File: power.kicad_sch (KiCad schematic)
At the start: 72 parts, among them J5 Molex_Mini-Fit-Jr_2x4_39-28-8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, Q1 DMPH4029LFGQ, Q12 SI7613DN-T1-GE3, Q13 SI7613DN-T1-GE3, Q2 BSS138-7-F, Q3 BSS138-7-F, U1 TPS56C230, U7 LTC4412IS6, U8 LTC4412IS6, U9 SIC477ED-T1-GE3

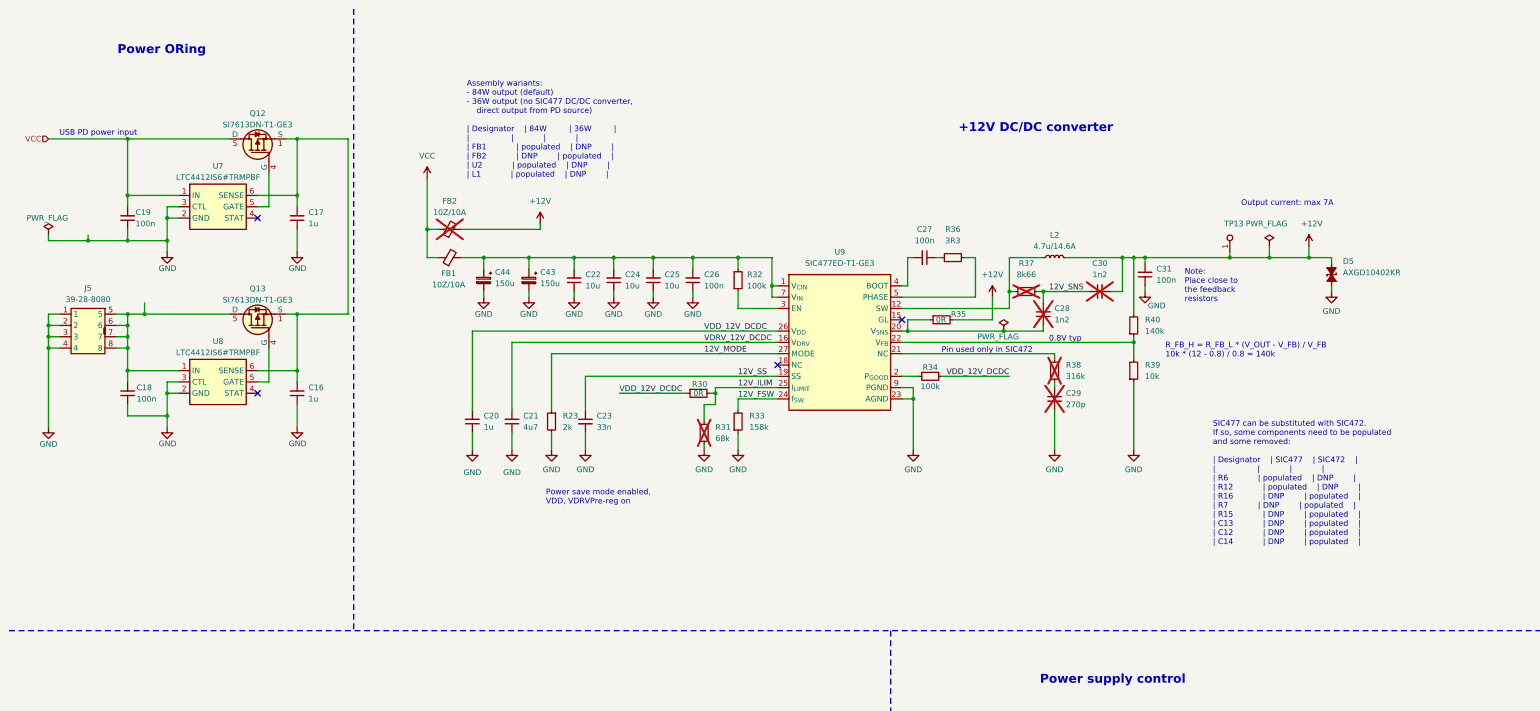
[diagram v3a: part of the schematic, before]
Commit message: [#79262] Move ideal diodes and Molex connector to separate schematic sheet
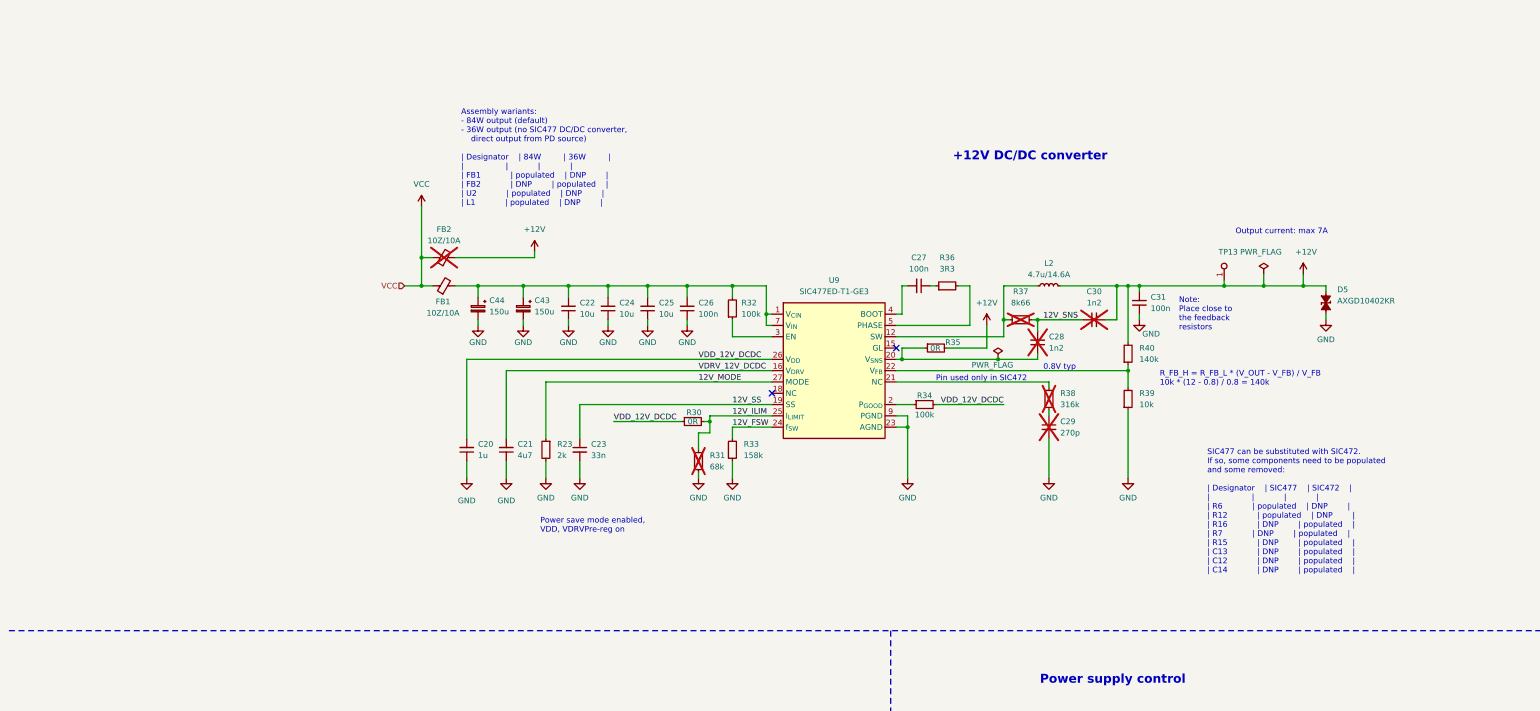
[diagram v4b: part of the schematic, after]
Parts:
- removed C16, C17: C_1u_25V_0603, antmicro-footprints:C_0603_1608Metric, symbol antmicroCapacitors0603:C_1u_25V_0603
- removed C18, C19: C_100n_0402, antmicro-footprints:C_0402_1005Metric, symbol antmicroCapacitors0402:C_100n_0402
- removed J5: Molex_Mini-Fit-Jr_2x4_39-28-8080, antmicro-footprints:MOLEX_39288080, symbol antmicroWire2BoardConnectors:Molex_Mini-Fit-Jr_2x4_39-28-8080
- removed Q12, Q13: SI7613DN-T1-GE3, antmicro-footprints:Vishay_PowerPAK_1212-8_Single, symbol antmicroTransistorsFETsMOSFETsSingle:SI7613DN-T1-GE3
- removed U7, U8: LTC4412IS6, antmicro-footprints:SOT-23-6, symbol antmicroPMICORControllersIdealDiodes:LTC4412IS6
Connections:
- no-connect marks 5 -> 3
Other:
- note removed: "Power ORing"
- note removed: "USB PD power input"
- moved on the sheet: C20, C21, C22, C23, C24, C25, C26, C27, C28, C29, C30, C31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

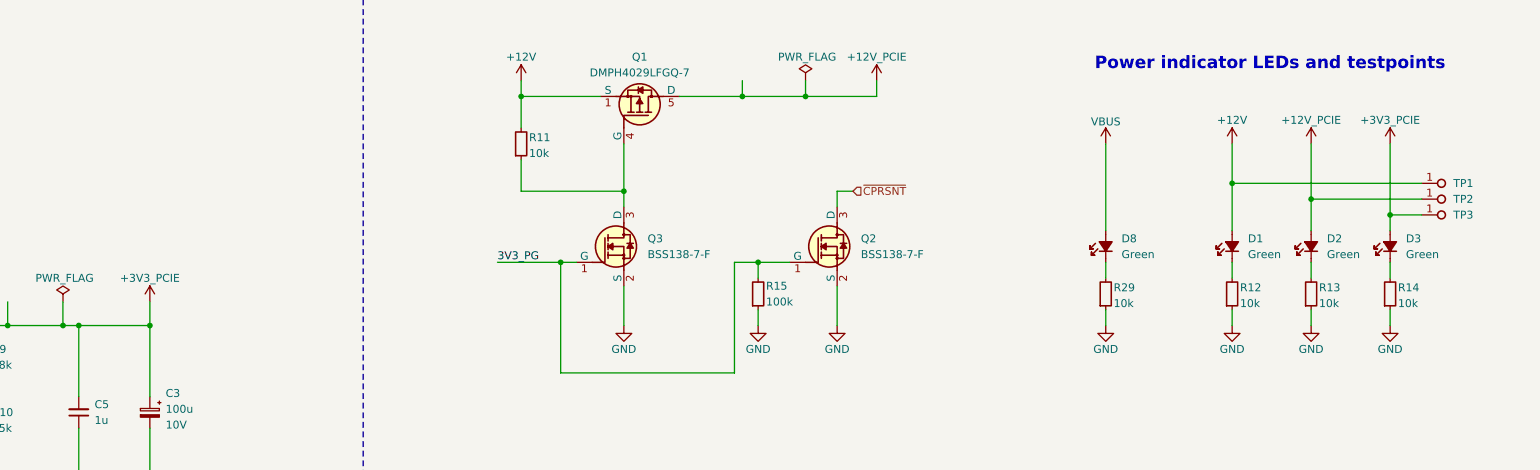
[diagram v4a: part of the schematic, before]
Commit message: [#79262] Change TVS diodes, adjust LEDs resistors, refactor USB-PD schematic
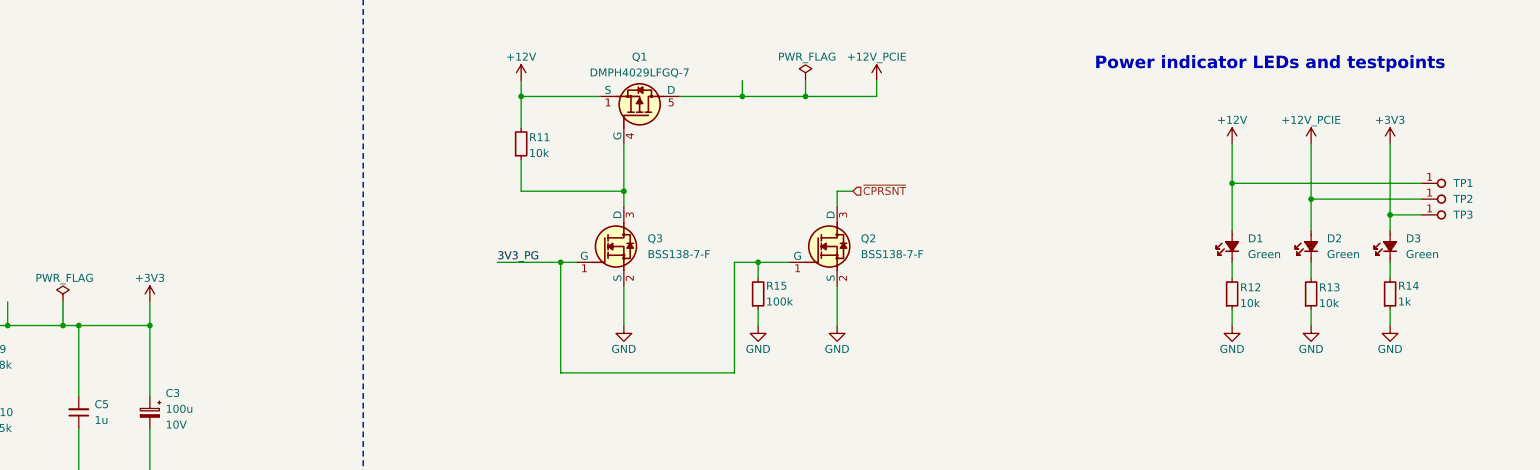
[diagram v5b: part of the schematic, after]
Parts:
- removed D8: LED_G_0603_LTST-C190GKT, antmicro-footprints:LED_0603_1608Metric_G, symbol antmicroLEDIndicationDiscrete:LED_G_0603_LTST-C190GKT
- removed R14, R29: R_10k_0402, antmicro-footprints:R_0402_1005Metric, symbol antmicroResistors0402:R_10k_0402
- added R14: R_1k_0402, antmicro-footprints:R_0402_1005Metric, symbol antmicroResistors0402:R_1k_0402
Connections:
- net GND: now also R14.1
- net at D3.1 (C): now also R14.2
- net +3V3_PCIE renamed +3V3

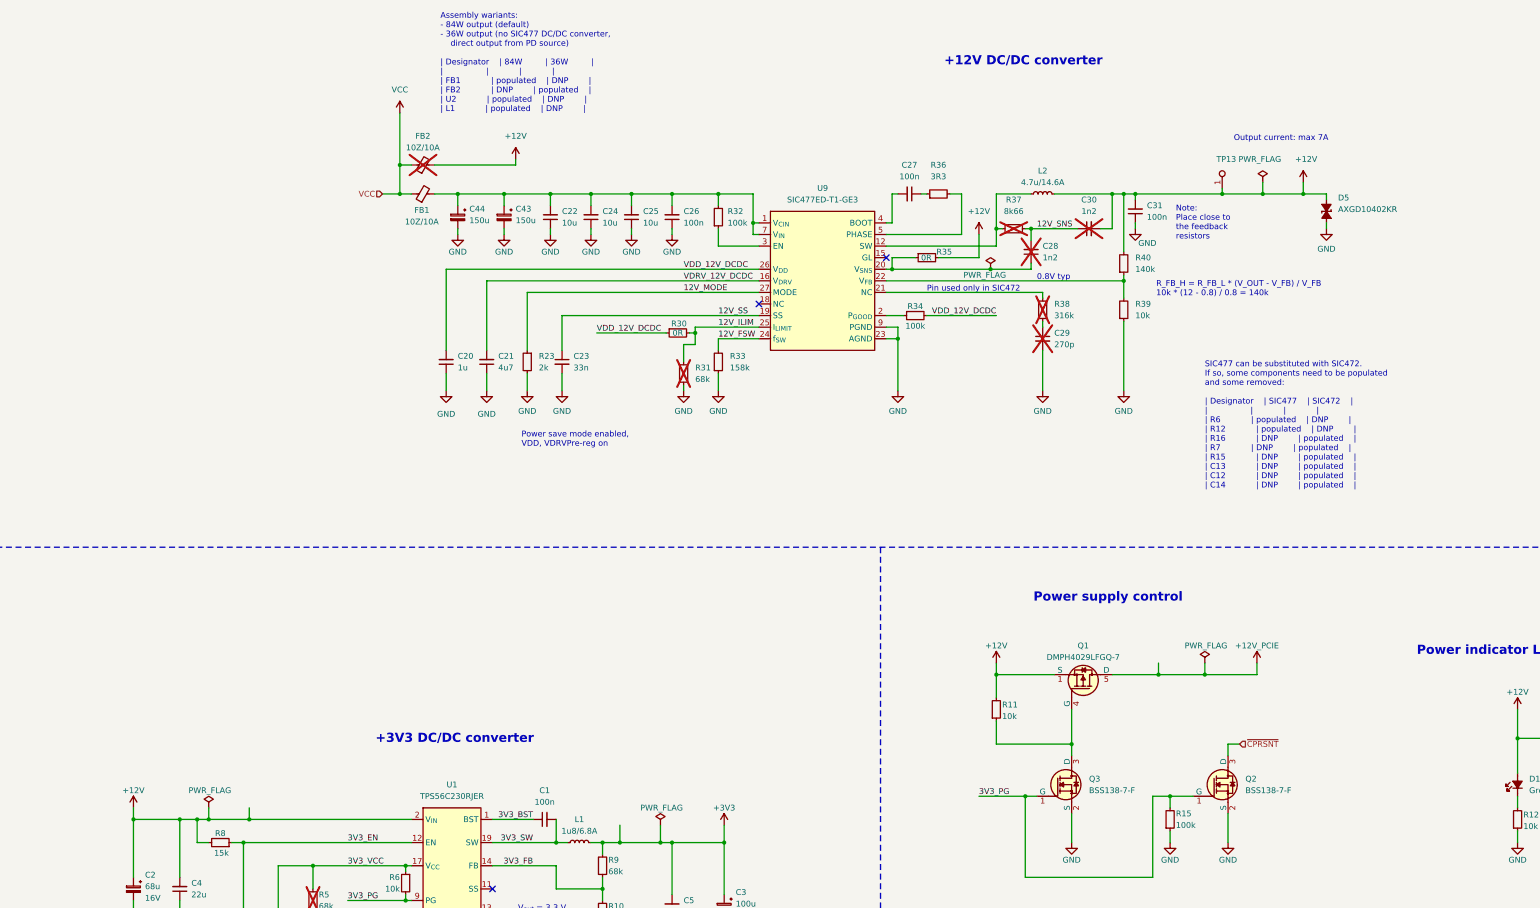
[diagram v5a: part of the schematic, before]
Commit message: [#79262] Cleanup 12V DC-DC converter, move Molex connector to root sheet
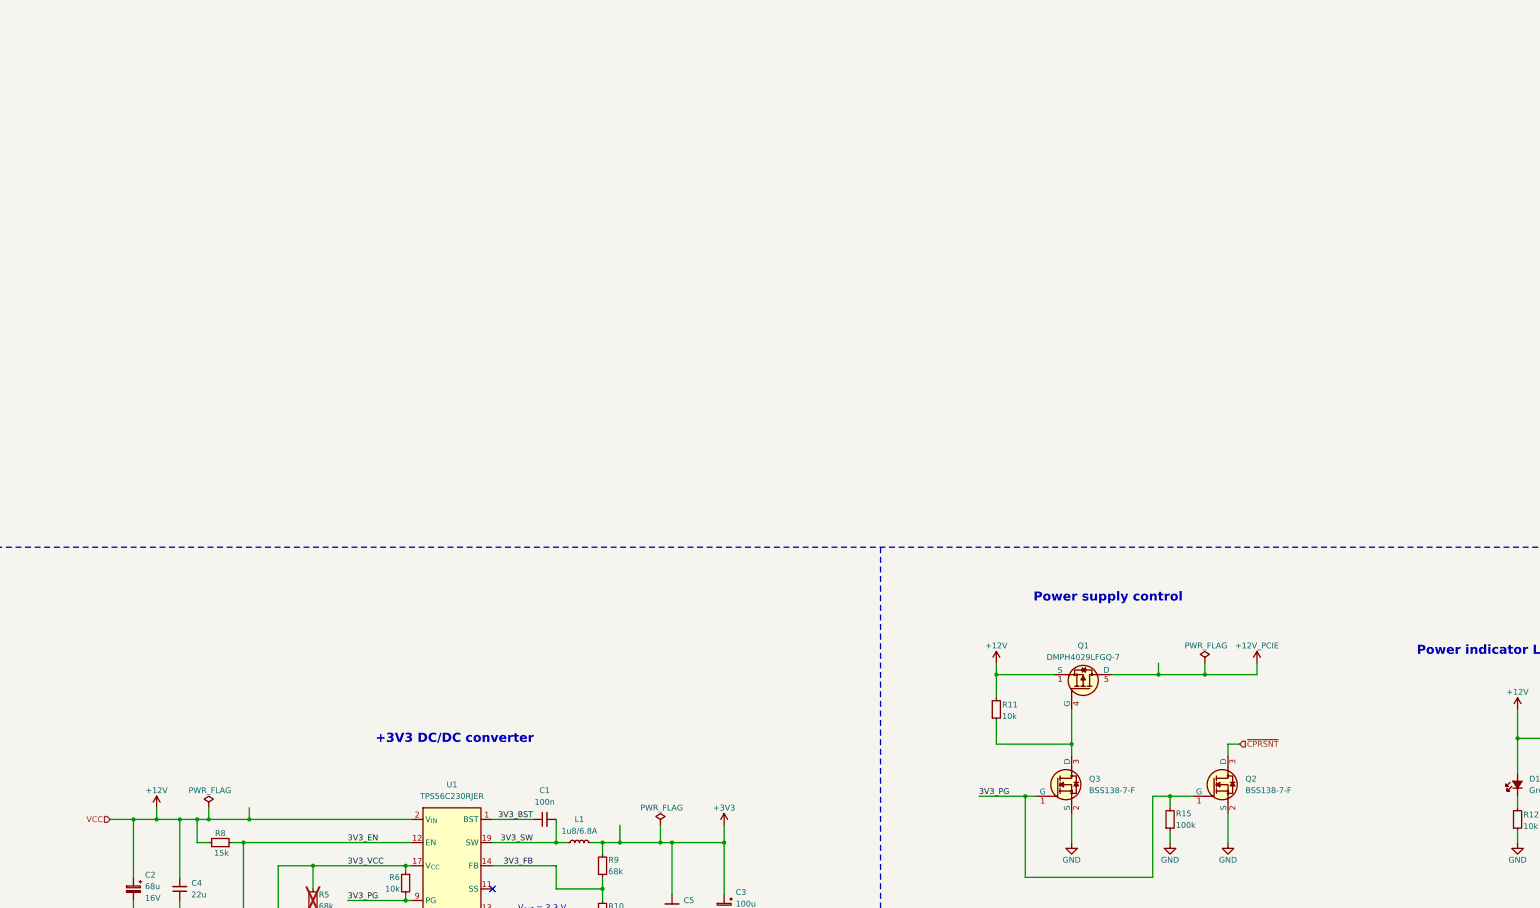
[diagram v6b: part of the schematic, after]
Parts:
- removed C20: C_1u_25V_0402, antmicro-footprints:C_0402_1005Metric, symbol antmicroCapacitors0402:C_1u_25V_0402
- removed C21: C_4u7_25V_0402, antmicro-footprints:C_0402_1005Metric, symbol antmicroCapacitors0402:C_4u7_25V_0402
- removed C22, C24, C25: C_10u_0805_35V, antmicro-footprints:C_0805_2012Metric, symbol antmicroCapacitorsmisc:C_10u_0805_35V
- removed C23: C_33n_0402, antmicro-footprints:C_0402_1005Metric, symbol antmicroCapacitors0402:C_33n_0402
- removed C26, C27, C31: C_100n_50V_X8L_0402, antmicro-footprints:C_0402_1005Metric, symbol antmicroCapacitors0402:C_100n_50V_X8L_0402
- removed C28, C30: C_1n2_50V_0402, antmicro-footprints:C_0402_1005Metric, symbol antmicroCapacitors0402:C_1n2_50V_0402
- removed C29: C_270p_25V_0402, antmicro-footprints:C_0402_1005Metric, symbol antmicroCapacitors0402:C_270p_25V_0402
- removed C43, C44: C_Pol_150u_30V_Vishay-T59-EE, antmicro-footprints:C_Pol_Vishay-T59-EE, symbol antmicroCapacitorspol:C_Pol_150u_30V_Vishay-T59-EE
- removed D5: AXGD10402KR, antmicro-footprints:D_0402_1005Metric, symbol antmicroTVSDiodes:AXGD10402KR
- removed FB1, FB2: FB_10Z_10A_WE-MPSB_1206, antmicro-footprints:FB_1206_3216Metric, symbol antmicroFerriteBeadsandChips:FB_10Z_10A_WE-MPSB_1206
- removed L2: L_4u7_14.6A_Abracon-Q8080, antmicro-footprints:L_Abracon_ASPIAIG-Q8080, symbol antmicroFixedInductors:L_4u7_14.6A_Abracon-Q8080
- removed R23: R_2k_0402, antmicro-footprints:R_0402_1005Metric, symbol antmicroResistors0402:R_2k_0402
- removed R30, R35: R_0R_0402, antmicro-footprints:R_0402_1005Metric, symbol antmicroResistors0402:R_0R_0402
- removed R31: R_68k_0402, antmicro-footprints:R_0402_1005Metric, symbol antmicroResistors0402:R_68k_0402
- removed R32, R34: R_100k_0402, antmicro-footprints:R_0402_1005Metric, symbol antmicroResistors0402:R_100k_0402
- removed R33: R_158k_0402, antmicro-footprints:R_0402_1005Metric, symbol antmicroResistors0402:R_158k_0402
- removed R36: R_3R3_0402, antmicro-footprints:R_0402_1005Metric, symbol antmicroResistors0402:R_3R3_0402
- removed R37: R_8k66_0402, antmicro-footprints:R_0402_1005Metric, symbol antmicroResistors0402:R_8k66_0402
- removed R38: R_316k_0402, antmicro-footprints:R_0402_1005Metric, symbol antmicroResistors0402:R_316k_0402
- removed R39: R_10k_0.1%_0402, antmicro-footprints:R_0402_1005Metric, symbol antmicroResistors0402:R_10k_0.1%_0402
- removed R40: R_140k_0.1%_0402, antmicro-footprints:R_0402_1005Metric, symbol antmicroResistors0402:R_140k_0.1%_0402
- removed TP13: TP_0.75mm_SMD, antmicro-footprints:TP_SMD_0.75mm, symbol antmicroTestPoints:TP_0.75mm_SMD
- removed U9: SIC477ED-T1-GE3, antmicro-footprints:SIC47XED-T1-GE3, symbol antmicroDCDCConverters:SIC477ED-T1-GE3
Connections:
- no-connect marks 3 -> 1
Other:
- note removed: "+12V DC/DC converter"
- note removed: "0.8V typ"
- note removed: "Assembly wariants: - 84W output (default) - 36W output (no SIC477 DC/DC converter, direct output from PD source) | Designator | 84W | 36W | | | | | | FB1 | populated | DNP | | FB2 | DNP | populated | | U2 | populated | DNP | | L1 | populated | DNP |"
- note removed: "Note: Place close to the feedback resistors"
- note removed: "Output current: max 7A"
- note removed: "Pin used only in SIC472"
- note removed: "Power save mode enabled, VDD, VDRVPre-reg on"
- note removed: "R_FB_H = R_FB_L * (V_OUT - V_FB) / V_FB 10k * (12 - 0.8) / 0.8 = 140k"
- note removed: "SIC477 can be substituted with SIC472. If so, some components need to be populated and some removed: | Designator | SIC477 | SIC472 | | | | | | R6 | populated | DNP | | R12 | populated | DNP | | R16 | DNP | populated | | R7 | DNP | populated | | R15 | DNP | populated | | C13 | DNP | populated | | C12 | DNP | populated | | C14 | DNP | populated |"

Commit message: [#79262] Finish power section schematic
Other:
- added sheet Ideal-diode-0 (ideal-diode.kicad_sch)
- added sheet Ideal-diode-1 (ideal-diode.kicad_sch)
- note added: "Power supply ORing"
- moved on the sheet: C1, C2, C3, C4, C5, C7, D1, D2, D3, L1, Q1, Q2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

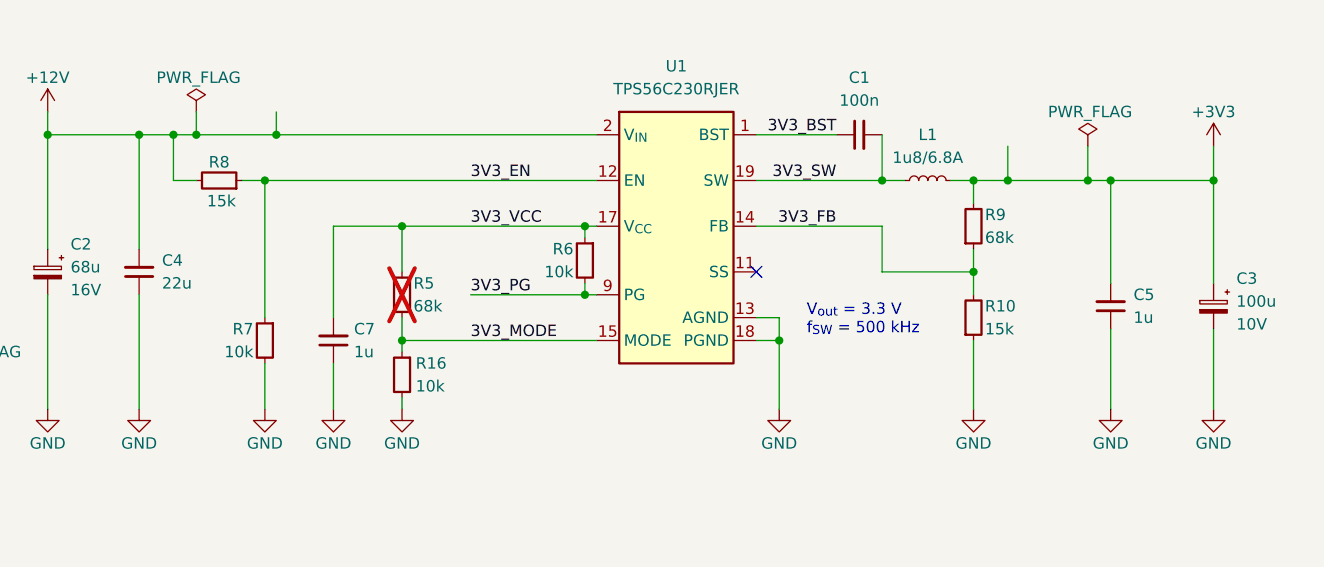
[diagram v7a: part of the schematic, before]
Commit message: [#79262] BOM consolidation
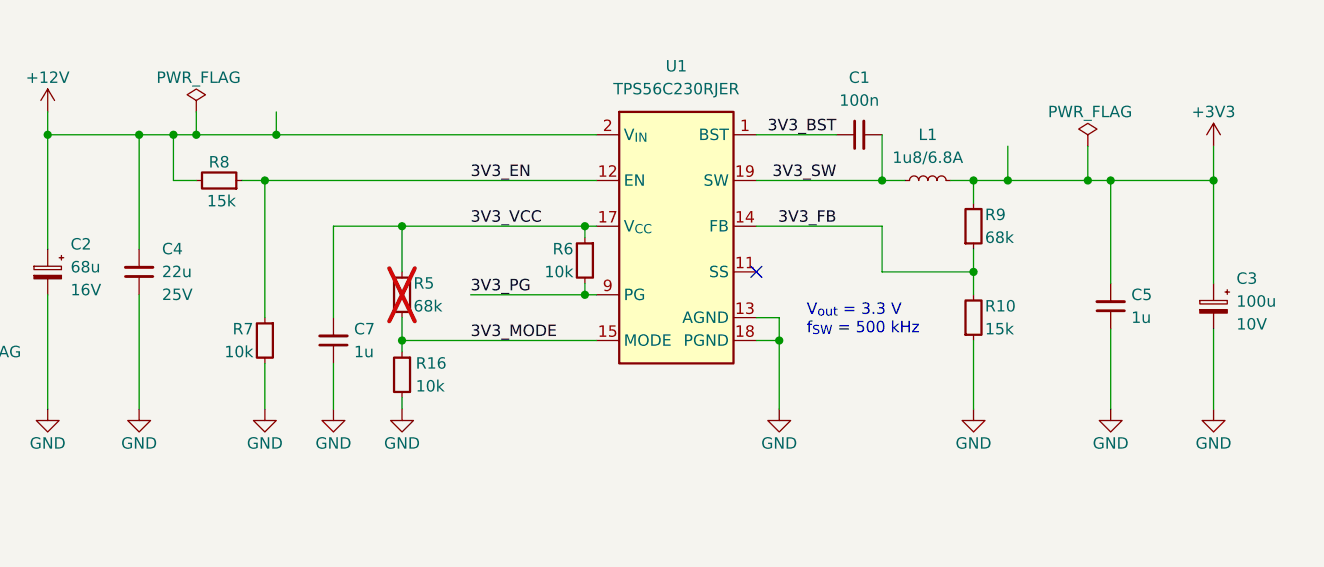
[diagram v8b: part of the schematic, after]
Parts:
- removed C4: C_22u_16V_0603, antmicro-footprints:C_0603_1608Metric_EIA, symbol antmicroCapacitors0603:C_22u_16V_0603
- removed C5, C7: C_1u_0402, antmicro-footprints:C_0402_1005Metric, symbol antmicroCapacitors0402:C_1u_0402
- added C4: C_22u_25V_0805, antmicro-footprints:C_0805_2012Metric, symbol antmicroCapacitorsmisc:C_22u_25V_0805
- added C5, C7: C_1u_25V_0402, antmicro-footprints:C_0402_1005Metric, symbol antmicroCapacitors0402:C_1u_25V_0402
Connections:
- net +12V: now also C4.2
- net +3V3: now also C5.2
- net 3V3_VCC: now also C7.2
- net GND: now also C4.1, C5.1, C7.1
